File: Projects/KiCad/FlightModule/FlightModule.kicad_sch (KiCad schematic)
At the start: 52 parts, among them J1 Conn_01x08, J2 Conn_01x02_Pin, J3 Conn_01x02_Pin, J4 Conn_01x02_Pin, J5 Conn_01x02_Pin, J6 Conn_01x02_Pin, SW1 SW_Push, SW2 SW_Push, U1 MCP2562-E-P, U2 NUCLEO-F303K8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

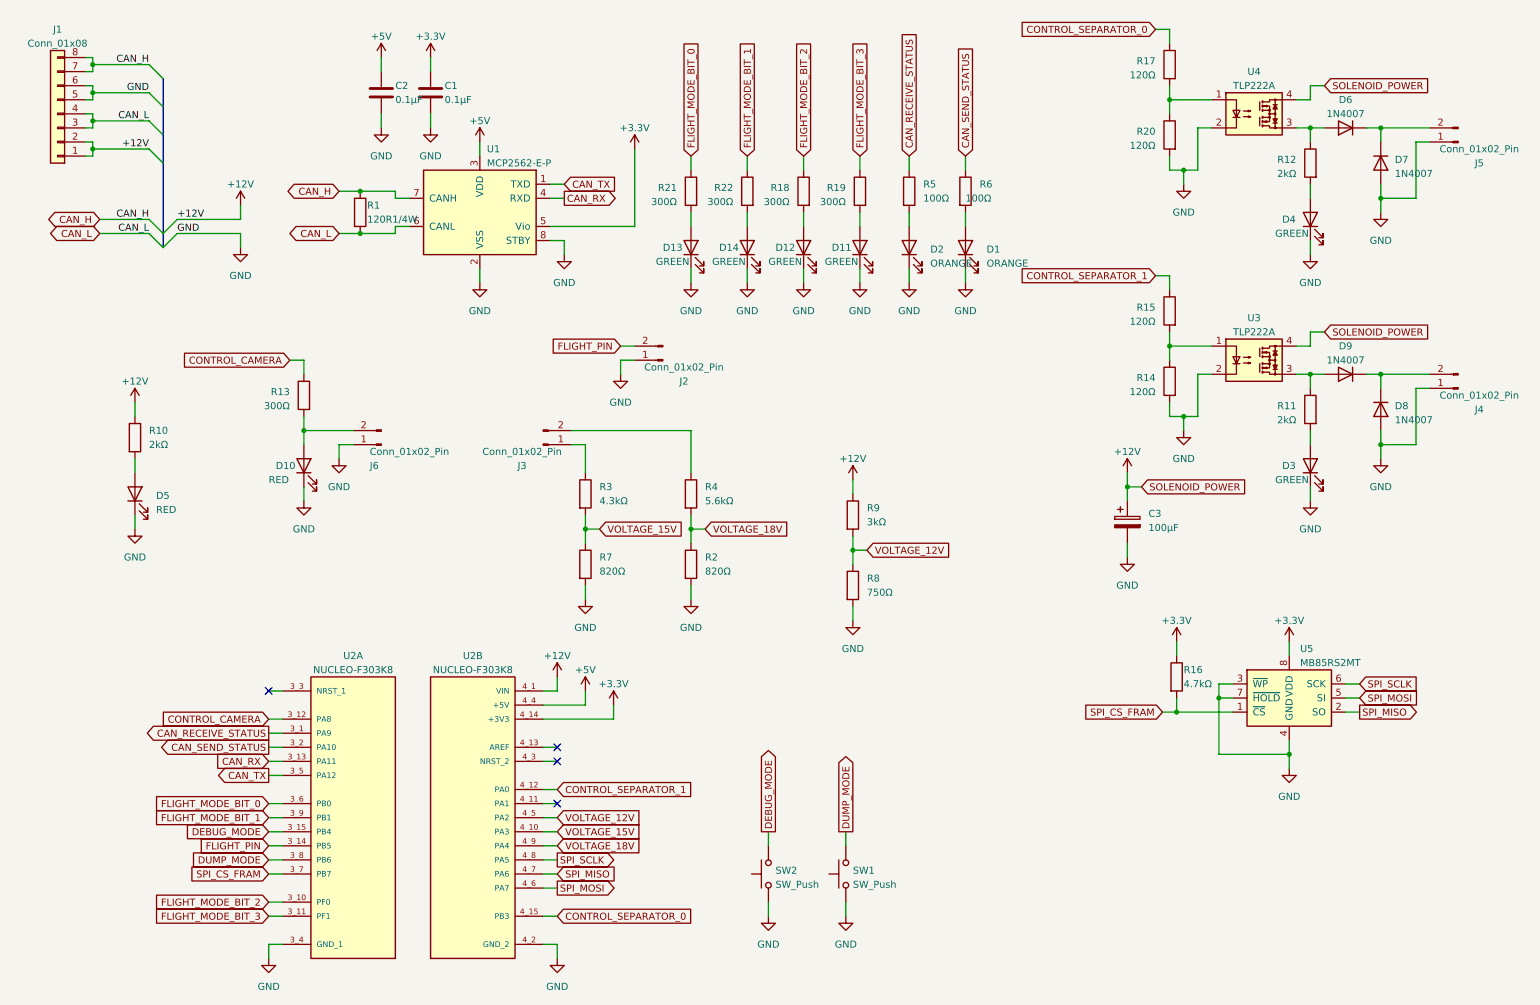
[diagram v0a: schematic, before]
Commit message: カメラの制御回路を修正
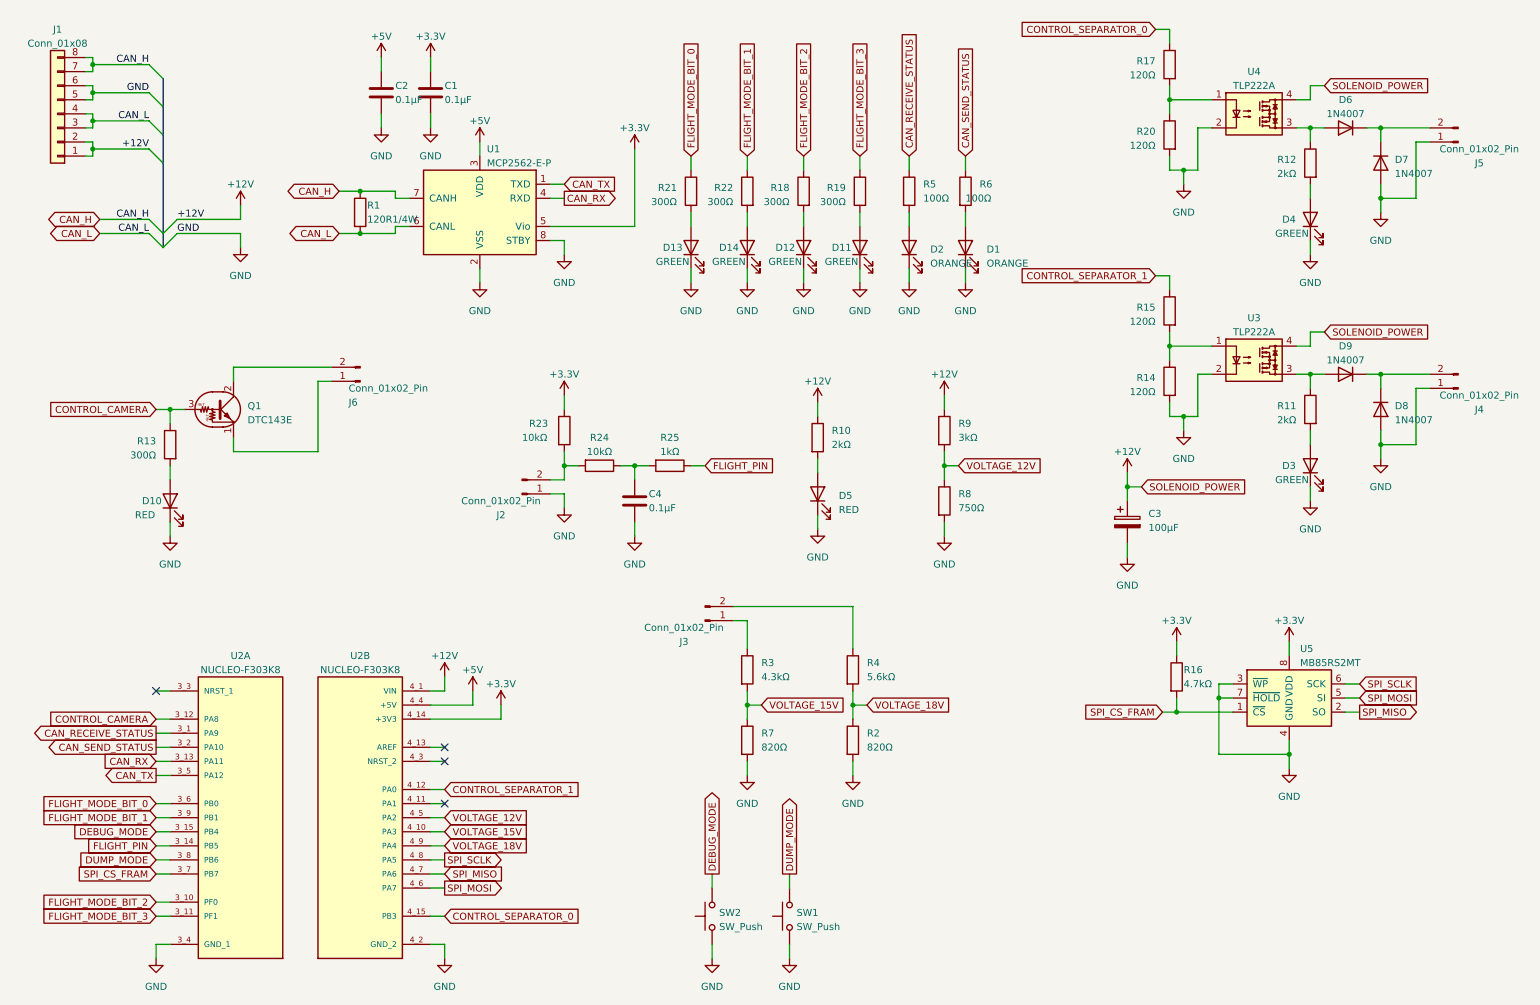
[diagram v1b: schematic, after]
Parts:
- added C4: 0.1μF, Capacitor_SMD:C_0805_2012Metric_Pad1.18x1.45mm_HandSolder, symbol Device:C
- added Q1: DTC143E, Package_TO_SOT_THT:TO-92_Inline, symbol Transistor_BJT:DTC143E
- added R23, R24: 10kΩ, Resistor_SMD:R_0603_1608Metric_Pad0.98x0.95mm_HandSolder, symbol Device:R
- added R25: 1kΩ, Resistor_SMD:R_0603_1608Metric_Pad0.98x0.95mm_HandSolder, symbol Device:R
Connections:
- net +3.3V: now also R23.1
- net CONTROL_CAMERA: now also Q1.3 (B)
- net FLIGHT_PIN: now also R25.1; no longer J2.2 (Pin_2)
- net GND: now also C4.2; no longer J6.1 (Pin_1)
- net at D10.2 (A), R13.2: no longer J6.2 (Pin_2)
- new net: C4.1, R24.1, R25.2
- new net: J6.1 (Pin_1), Q1.1 (E)
- new net: J6.2 (Pin_2), Q1.2 (C)
- new net: J2.2 (Pin_2), R23.2, R24.2
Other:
- moved on the sheet: D10, D5, J2, J3, J6, R10, R2, R3, R4, R7, R8, R9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

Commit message: ソレノイドのサージ対策回路を修正
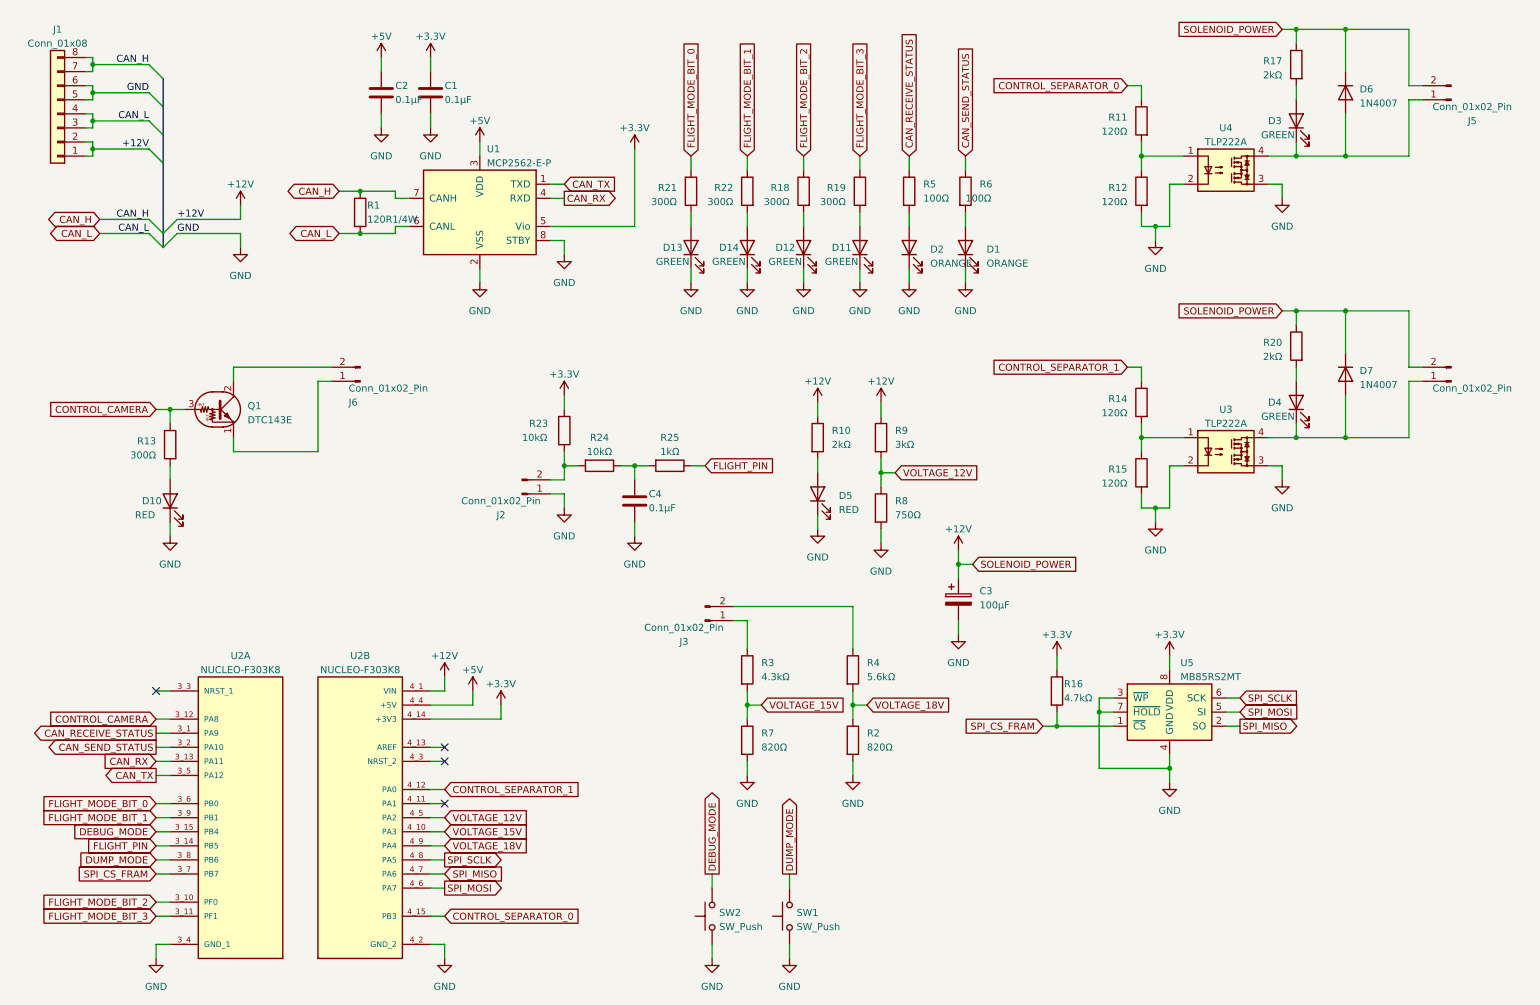
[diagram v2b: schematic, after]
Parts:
- removed D3: GREEN, LED_SMD:LED_0603_1608Metric_Pad1.05x0.95mm_HandSolder, symbol Device:LED
- removed D8, D9: 1N4007, Diode_SMD:D_SOD-123F, symbol Diode:1N4007
- removed R11: 2kΩ, Resistor_SMD:R_0603_1608Metric_Pad0.98x0.95mm_HandSolder, symbol Device:R
- added D4: GREEN, LED_SMD:LED_0603_1608Metric_Pad1.05x0.95mm_HandSolder, symbol Device:LED
- added R20: 2kΩ, Resistor_SMD:R_0603_1608Metric_Pad0.98x0.95mm_HandSolder, symbol Device:R
- renumbered D4 to D3, R17 to R11, R20 to R12, R12 to R17
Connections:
- net +12V: now also D6.1 (K), D7.1 (K), J4.2 (Pin_2), J5.2 (Pin_2), R17.1, R20.1; no longer U3.4, U4.4
- net CONTROL_SEPARATOR_1: now also R14.1; no longer R15.1
- net GND: now also R15.2, U3.3, U4.3; no longer D3.1 (K), D7.2 (A), J4.1 (Pin_1), J5.1 (Pin_1), R14.2
- new net: R14.2, R15.1, U3.1
- new net: D3.1 (K), D6.2 (A), J5.1 (Pin_1), U4.4
- new net: D4.1 (K), D7.2 (A), J4.1 (Pin_1), U3.4
- new net: D4.2 (A), R20.2
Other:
- moved on the sheet: C3, D3, D6, J5, R11, R12, R16, R17, R8, R9, U4, U5

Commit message: テストポイントを追加
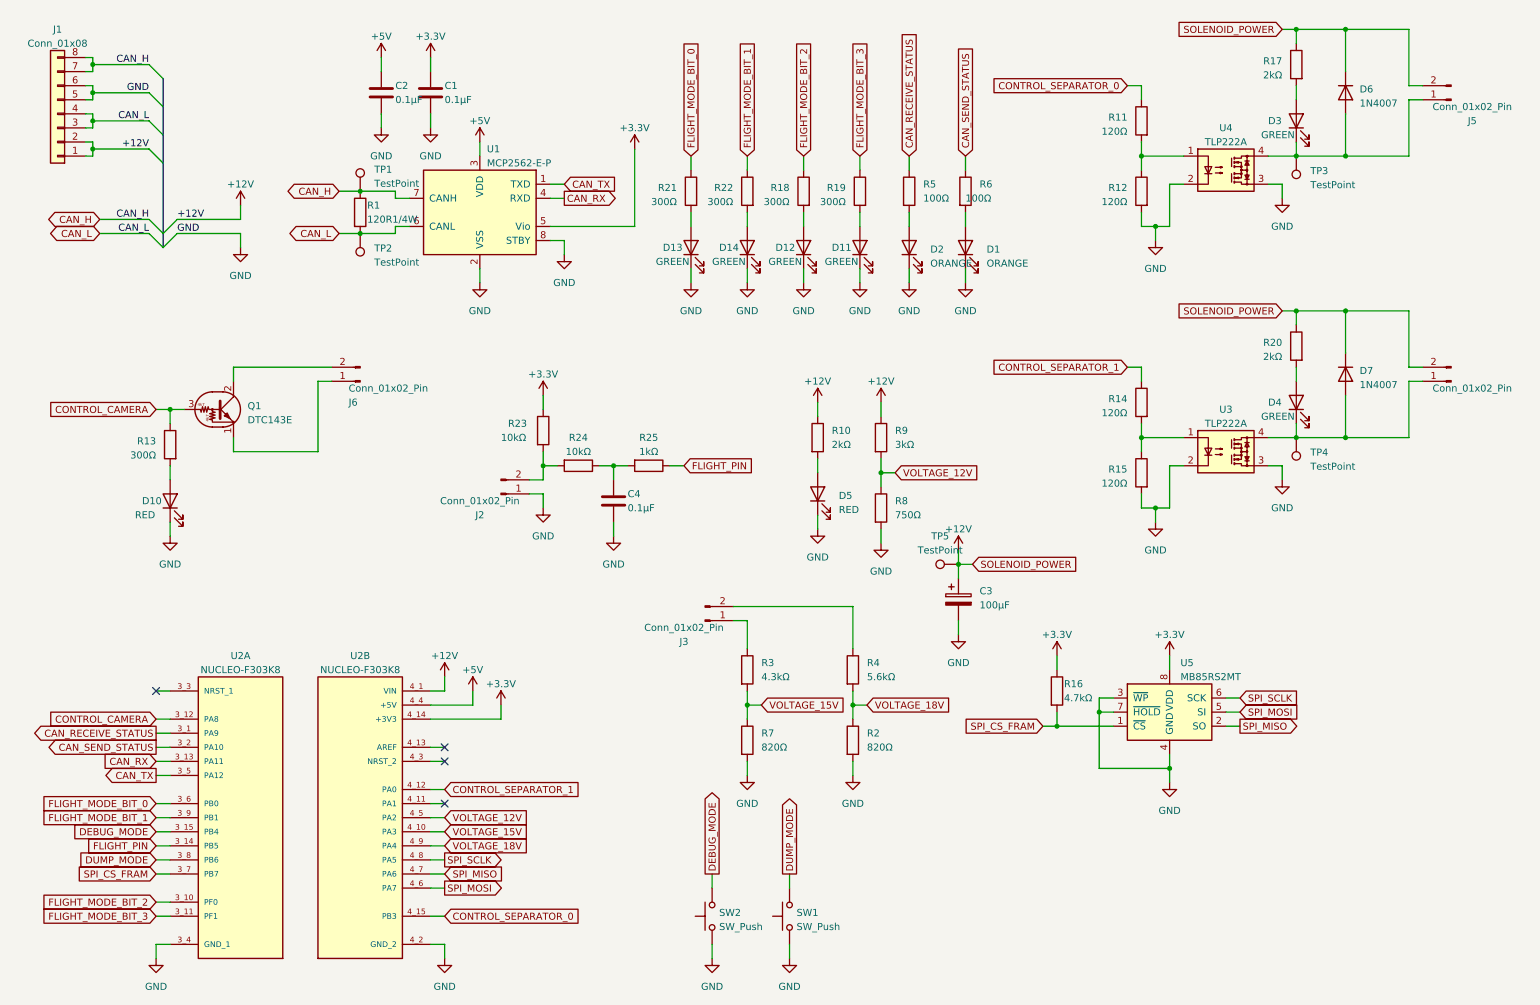
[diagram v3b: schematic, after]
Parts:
- added TP1, TP2, TP3, TP4, TP5: TestPoint, Connector_Pin:Pin_D1.0mm_L10.0mm, symbol Connector:TestPoint
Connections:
- net +12V: now also TP5.1
- net CAN_H: now also TP1.1
- net CAN_L: now also TP2.1
- net at D3.1 (K), D6.2 (A), J5.1 (Pin_1)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: now also TP3.1
- net at D4.1 (K), D7.2 (A), J4.1 (Pin_1)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: now also TP4.1
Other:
- moved on the sheet: C4, J2, R23, R24, R25
